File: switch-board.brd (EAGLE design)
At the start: 100 x 80 mm, 5 parts

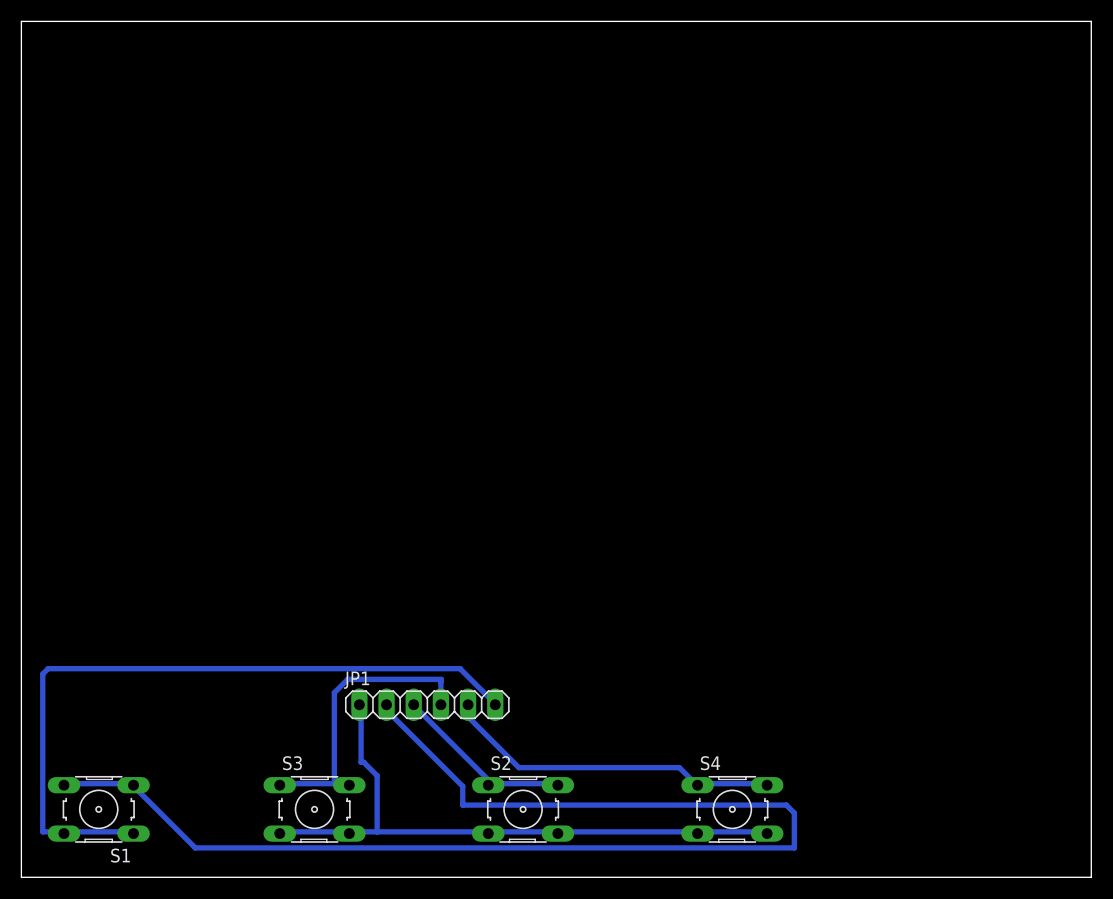
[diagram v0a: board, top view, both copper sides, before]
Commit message: Mounting holes added
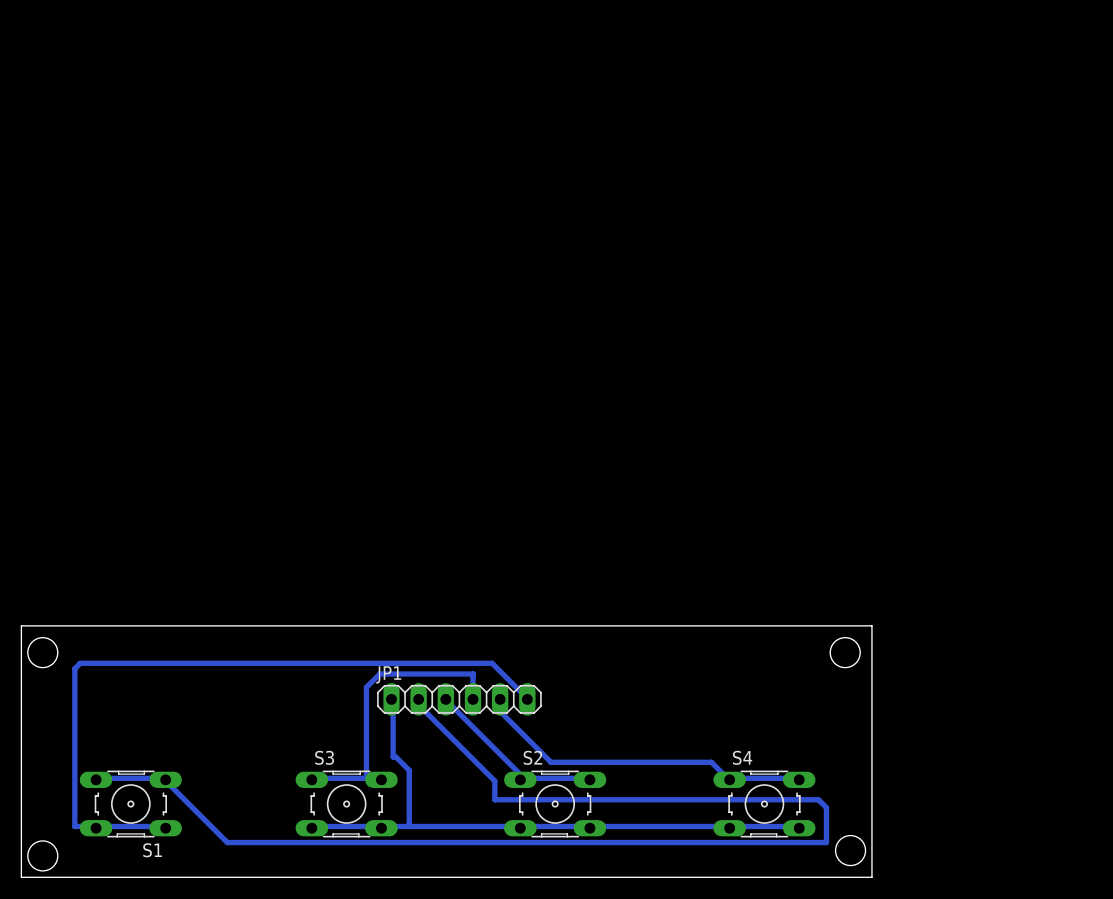
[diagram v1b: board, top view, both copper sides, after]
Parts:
- moved JP1 3.04 mm to (40.9, 16.6)
- moved S1 3.04 mm to (10.2, 6.85)
- moved S2 3.04 mm to (49.9, 6.85)
- moved S3 3.04 mm to (30.4, 6.85)
- moved S4 3.04 mm to (69.5, 6.85)
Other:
- board size 100 x 80 mm -> 79.5 x 23.5 mm
